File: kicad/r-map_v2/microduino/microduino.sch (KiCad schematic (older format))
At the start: 14 parts, among them P1 CONN_01X02, P2 CONN_RELE_BOARD, P3 CONN_01X05, P4 CONFIG, P5 USB_OTG, U1 Microduino, U2 ESDA6V1-5SC6, U3 LP2985LV, U4 TMP275

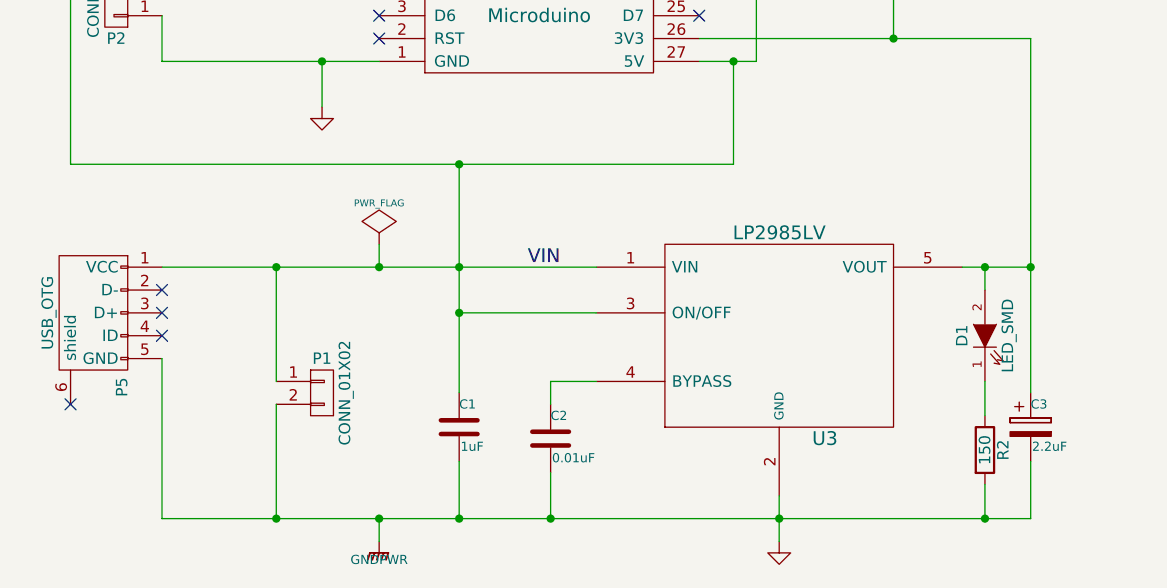
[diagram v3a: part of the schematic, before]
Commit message: Aggiunto ponticello a saldare per uscita 3.3V. Nuovo design per i2chub
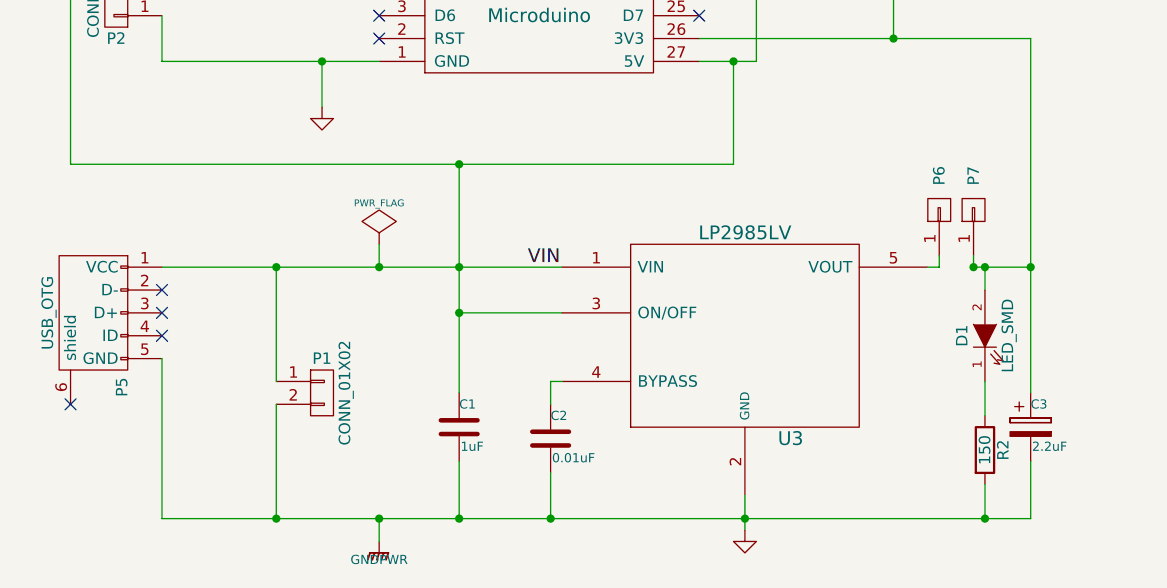
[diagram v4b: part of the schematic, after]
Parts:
- added P6, P7: CONN_01X01, Measurement_Points:Measurement_Point_Square-SMD-Pad_Small, symbol CONN_01X01
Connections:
- net +3.3V: now also P7.1 (P1); no longer U3.5 (VOUT)
- new net: P6.1 (P1), U3.5 (VOUT)
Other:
- moved on the sheet: U3
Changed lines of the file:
@@
 L LP2985LV U3
 U 1 1 548EC800
-P 5450 6400
-F 0 "U3" H 5650 5950 60  0000 C CNN
-F 1 "LP2985LV" H 5450 6850 60  0000 C CNN
-F 2 "w_smd_trans:sot23-5" H 5450 6400 60  0001 C CNN
-F 3 "http://www.ti.com/lit/ds/symlink/lp2985-n.pdf" H 5450 6400 60  0001 C CNN
-	1    5450 6400
+P 5300 6400
+F 0 "U3" H 5500 5950 60  0000 C CNN
+F 1 "LP2985LV" H 5300 6850 60  0000 C CNN
+F 2 "w_smd_trans:sot23-5" H 5300 6400 60  0001 C CNN
+F 3 "http://www.ti.com/lit/ds/symlink/lp2985-n.pdf" H 5300 6400 60  0001 C CNN
+	1    5300 6400
 	1    0    0    -1
 $EndComp
@@
 L GND #PWR01
 U 1 1 548ECA52
-P 5450 7300
-F 0 "#PWR01" H 5450 7300 30  0001 C CNN
-F 1 "GND" H 5450 7230 30  0001 C CNN
-F 2 "" H 5450 7300 60  0000 C CNN
-F 3 "" H 5450 7300 60  0000 C CNN
-	1    5450 7300
+P 5300 7250
+F 0 "#PWR01" H 5300 7250 30  0001 C CNN
+F 1 "GND" H 5300 7180 30  0001 C CNN
+F 2 "" H 5300 7250 60  0000 C CNN
+F 3 "" H 5300 7250 60  0000 C CNN
+	1    5300 7250
 	1    0    0    -1
 $EndComp
@@
 $EndComp
 NoConn ~ 3700 4500
-Wire Wire Line
-	2750 5200 3700 5200
-Wire Wire Line
-	4600 3750 4050 3750
-Wire Wire Line
-	4300 3750 4300 4000
-Wire Wire Line
-	2850 2900 5800 2900
-Wire Wire Line
-	4800 2750 4800 3250
-Wire Wire Line
-	5950 5100 5950 3250
-Wire Wire Line
-	3000 3550 2850 3550
-Wire Wire Line
-	4200 3550 4200 4000
-Wire Wire Line
-	2750 5200 2750 5000
-Wire Wire Line
-	2750 4900 3700 4900
-Wire Wire Line
-	3700 4800 2750 4800
-Wire Wire Line
-	2850 3550 2850 2900
-Wire Wire Line
-	5250 5650 5250 5200
-Wire Wire Line
-	2350 5650 5250 5650
-Wire Wire Line
-	2350 5650 2350 4400
-Wire Wire Line
-	2350 4400 2750 4400
-Wire Wire Line
-	2750 4400 2750 4500
-Wire Wire Line
-	4600 2750 4600 3750
-Wire Wire Line
-	4500 3550 4500 2750
-Wire Wire Line
-	4700 2900 4700 2750
-Wire Wire Line
-	4400 2750 4400 3350
-Wire Wire Line
-	4050 3350 5350 3350
-Wire Wire Line
-	5350 3350 5350 5200
-Connection ~ 5250 5200
-Wire Wire Line
-	5950 3250 4800 3250
-Wire Wire Line
-	4050 3550 4500 3550
-Connection ~ 4200 3550
-Connection ~ 4300 3750
-Wire Wire Line
-	4050 7200 4050 6950
-Wire Wire Line
-	2750 7200 6550 7200
-Wire Wire Line
-	6550 7200 6550 6950
-Wire Wire Line
-	5450 7100 5450 7300
-Connection ~ 5450 7200
-Wire Wire Line
-	6550 5100 6550 6650
-Wire Wire Line
-	4050 5650 4050 6650
-Wire Wire Line
-	2750 6100 4650 6100
-Wire Wire Line
-	4050 6300 4650 6300
-Connection ~ 4050 6300
-Wire Wire Line
-	6250 6100 6550 6100
-Connection ~ 4050 7200
-Connection ~ 4050 6100
-Wire Wire Line
-	3250 6600 3250 6100
-Connection ~ 3250 6100
-Wire Wire Line
-	3250 6700 3250 7200
-Connection ~ 3250 7200
-Wire Wire Line
-	4650 6600 4450 6600
-Wire Wire Line
-	4450 6600 4450 6700
-Wire Wire Line
-	4450 7000 4450 7200
-Connection ~ 4450 7200
-Connection ~ 6550 6100
-Wire Wire Line
-	3700 6000 3700 6100
-Connection ~ 3700 6100
-Wire Wire Line
-	3700 7300 3700 7200
-Connection ~ 3700 7200
-Wire Wire Line
-	5850 3000 4500 3000
-Connection ~ 4500 3000
-Wire Wire Line
-	5850 3150 4600 3150
-Connection ~ 4600 3150
-Wire Wire Line
-	5800 2900 5800 4400
-Wire Wire Line
-	7050 3850 5800 3850
-Connection ~ 4700 2900
-Wire Wire Line
-	3000 2800 5650 2800
-Wire Wire Line
-	5650 2800 5650 2550
-Wire Wire Line
-	5650 2550 6350 2550
-Wire Wire Line
-	6350 2550 6350 2600
-Connection ~ 4800 2800
-Wire Wire Line
-	6850 2900 7050 2900
-Wire Wire Line
-	7050 2900 7050 3850
-Connection ~ 6350 3850
-Wire Wire Line
-	6850 3000 7050 3000
-Connection ~ 7050 3000
-Wire Wire Line
-	6850 3100 7050 3100
-Wire Wire Line
-	5100 4900 5800 4900
-Connection ~ 5800 3850
-Connection ~ 4050 5650
-Wire Wire Line
-	3450 5200 3450 5400
-Connection ~ 3450 5200
-Wire Wire Line
-	5100 5100 6550 5100
-Wire Wire Line
-	5350 5200 5100 5200
-Wire Wire Line
-	6350 3750 6350 4000
 NoConn ~ 2750 6400
 $Comp
@@
 	0    -1   1    0
 $EndComp
-Wire Wire Line
-	2750 7200 2750 6500
 NoConn ~ 2350 6700
 $Comp
@@
 	1    0    0    -1
 $EndComp
-Wire Wire Line
-	6350 6750 6350 6600
-Wire Wire Line
-	6350 6200 6350 6100
-Connection ~ 6350 6100
-Wire Wire Line
-	6350 7050 6350 7200
-Connection ~ 6350 7200
 Text Label 4300 3550 0    60   ~ 0
 SCL
 Text Label 4400 3750 0    60   ~ 0
 SDA
-Connection ~ 7050 3100
 Text Label 5350 2800 0    60   ~ 0
 +3.3V
@@
 Text Label 4350 6100 0    60   ~ 0
 VIN
+NoConn ~ 3700 4600
+NoConn ~ 3700 4700
+Wire Wire Line
+	2750 5200 3700 5200
+Wire Wire Line
+	4600 3750 4050 3750
+Wire Wire Line
+	4300 3750 4300 4000
+Wire Wire Line
+	2850 2900 5800 2900
+Wire Wire Line
+	4800 2750 4800 3250
+Wire Wire Line
+	5950 5100 5950 3250
+Wire Wire Line
+	3000 3550 2850 3550
+Wire Wire Line
+	4200 3550 4200 4000
+Wire Wire Line
+	2750 5200 2750 5000
+Wire Wire Line
+	2750 4900 3700 4900
+Wire Wire Line
+	3700 4800 2750 4800
+Wire Wire Line
+	2850 3550 2850 2900
+Wire Wire Line
+	5250 5650 5250 5200
+Wire Wire Line
+	2350 5650 5250 5650
+Wire Wire Line
+	2350 5650 2350 4400
+Wire Wire Line
+	2350 4400 2750 4400
+Wire Wire Line
+	2750 4400 2750 4500
+Wire Wire Line
+	4600 2750 4600 3750
+Wire Wire Line
+	4500 3550 4500 2750
+Wire Wire Line
+	4700 2900 4700 2750
+Wire Wire Line
+	4400 2750 4400 3350
+Wire Wire Line
+	4050 3350 5350 3350
+Wire Wire Line
+	5350 3350 5350 5200
+Connection ~ 5250 5200
+Wire Wire Line
+	5950 3250 4800 3250
+Wire Wire Line
+	4050 3550 4500 3550
+Connection ~ 4200 3550
+Connection ~ 4300 3750
+Wire Wire Line
+	4050 7200 4050 6950
+Wire Wire Line
+	2750 7200 6550 7200
+Wire Wire Line
+	6550 7200 6550 6950
+Wire Wire Line
+	5300 7100 5300 7250
+Connection ~ 5300 7200
+Wire Wire Line
+	6550 5100 6550 6650
+Wire Wire Line
+	4050 5650 4050 6650
+Wire Wire Line
+	2750 6100 4500 6100
+Wire Wire Line
+	4050 6300 4500 6300
+Connection ~ 4050 6300
+Connection ~ 4050 7200
+Connection ~ 4050 6100
+Wire Wire Line
+	3250 6600 3250 6100
+Connection ~ 3250 6100
+Wire Wire Line
+	3250 6700 3250 7200
+Connection ~ 3250 7200
+Wire Wire Line
+	4500 6600 4450 6600
+Wire Wire Line
+	4450 6600 4450 6700
+Wire Wire Line
+	4450 7000 4450 7200
+Connection ~ 4450 7200
+Connection ~ 6550 6100
+Wire Wire Line
+	3700 6000 3700 6100
+Connection ~ 3700 6100
+Wire Wire Line
+	3700 7300 3700 7200
+Connection ~ 3700 7200
+Wire Wire Line
+	5850 3000 4500 3000
+Connection ~ 4500 3000
+Wire Wire Line
+	5850 3150 4600 3150
+Connection ~ 4600 3150
+Wire Wire Line
+	5800 2900 5800 4400
+Wire Wire Line
+	7050 3850 5800 3850
+Connection ~ 4700 2900
+Wire Wire Line
+	3000 2800 5650 2800
+Wire Wire Line
+	5650 2800 5650 2550
+Wire Wire Line
+	5650 2550 6350 2550
+Wire Wire Line
+	6350 2550 6350 2600
+Connection ~ 4800 2800
+Wire Wire Line
+	6850 2900 7050 2900
+Wire Wire Line
+	7050 2900 7050 3850
+Connection ~ 6350 3850
+Wire Wire Line
+	6850 3000 7050 3000
+Connection ~ 7050 3000
+Wire Wire Line
+	6850 3100 7050 3100
+Wire Wire Line
+	5100 4900 5800 4900
+Connection ~ 5800 3850
+Connection ~ 4050 5650
+Wire Wire Line
+	3450 5200 3450 5400
+Connection ~ 3450 5200
+Wire Wire Line
+	5100 5100 6550 5100
+Wire Wire Line
+	5350 5200 5100 5200
+Wire Wire Line
+	6350 3750 6350 4000
+Wire Wire Line
+	2750 7200 2750 6500
+Wire Wire Line
+	6350 6750 6350 6600
+Wire Wire Line
+	6350 6200 6350 6100
+Connection ~ 6350 6100
+Wire Wire Line
+	6350 7050 6350 7200
+Connection ~ 6350 7200
+Connection ~ 7050 3100
 Connection ~ 5950 5100
 Connection ~ 4400 3350
@@
 Wire Wire Line
 	3550 4600 2750 4600
-NoConn ~ 3700 4600
-NoConn ~ 3700 4700
+$Comp
+L CONN_01X01 P6
+U 1 1 55F70AFE
+P 6150 5850
+F 0 "P6" H 6300 5850 50  0000 C CNN
+F 1 "CONN_01X01" V 6250 5850 50  0001 C CNN
+F 2 "Measurement_Points:Measurement_Point_Square-SMD-Pad_Small" H 6150 5850 60  0001 C CNN
+F 3 "" H 6150 5850 60  0000 C CNN
+	1    6150 5850
+	0    -1   -1   0
+$EndComp
+$Comp
+L CONN_01X01 P7
+U 1 1 55F70BDA
+P 6300 5850
+F 0 "P7" H 6450 5850 50  0000 C CNN
+F 1 "CONN_01X01" V 6400 5850 50  0001 C CNN
+F 2 "Measurement_Points:Measurement_Point_Square-SMD-Pad_Small" H 6300 5850 60  0001 C CNN
+F 3 "" H 6300 5850 60  0000 C CNN
+	1    6300 5850
+	0    -1   -1   0
+$EndComp
+Wire Wire Line
+	6300 6050 6300 6100
+Connection ~ 6300 6100
+Wire Wire Line
+	6150 6050 6150 6100
+Wire Wire Line
+	6150 6100 6100 6100
+Wire Wire Line
+	6300 6100 6550 6100
 $EndSCHEMATC

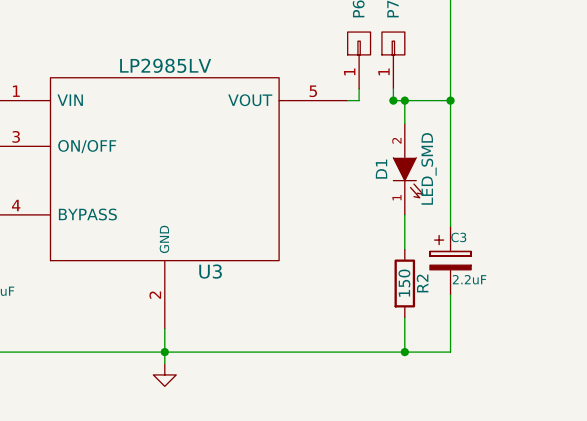
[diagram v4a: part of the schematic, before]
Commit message: Aggiornamento files gerber e verifica per nuova stampa pcb, revisionate tutte e 4 le board. Il file kicad/r-map_v2/futura_10-2015.zip contiene i files divisi per cartelle di tutte le board
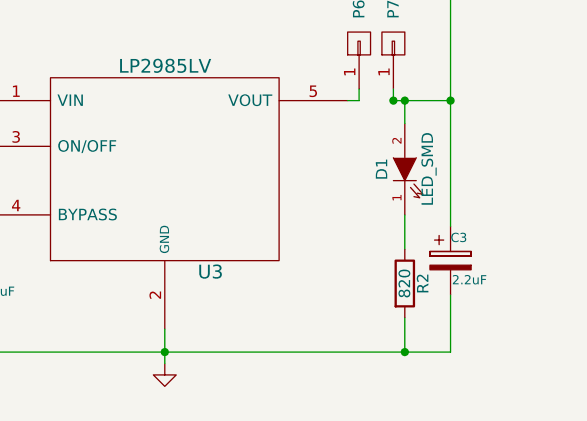
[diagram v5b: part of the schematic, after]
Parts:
- R2: value 150 -> 820
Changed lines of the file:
@@
 P 6350 6900
 F 0 "R2" V 6430 6900 50  0000 C CNN
-F 1 "150" V 6350 6900 50  0000 C CNN
+F 1 "820" V 6350 6900 50  0000 C CNN
 F 2 "w_smd_resistors:r_1206" V 6280 6900 30  0001 C CNN
 F 3 "" H 6350 6900 30  0000 C CNN

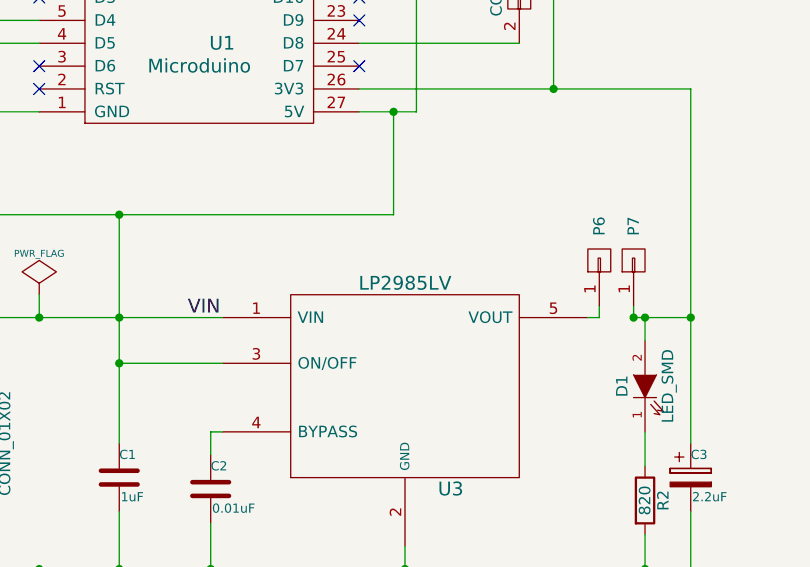
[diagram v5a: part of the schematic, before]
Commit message: Aggiornamento lista componenti e cancellazione vecchi files
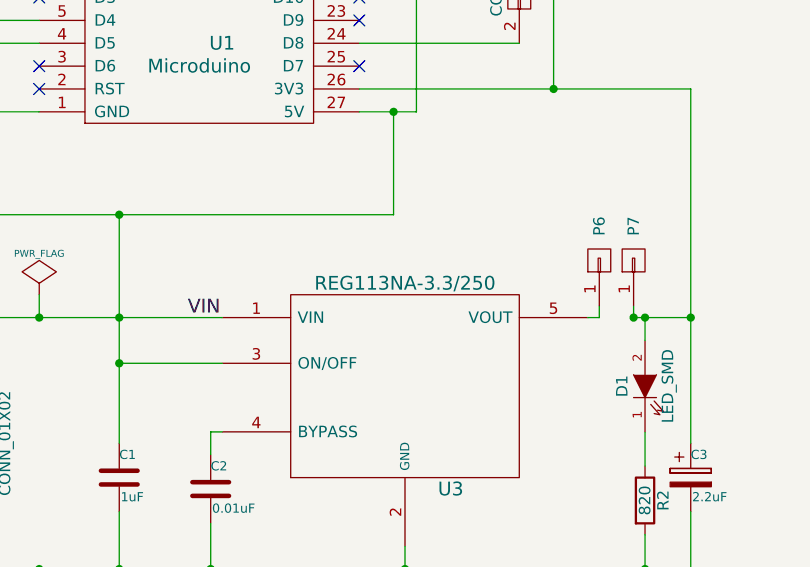
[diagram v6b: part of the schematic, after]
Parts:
- U3: value LP2985LV -> REG113NA-3.3/250
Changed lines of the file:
@@
 P 5300 6400
 F 0 "U3" H 5500 5950 60  0000 C CNN
-F 1 "LP2985LV" H 5300 6850 60  0000 C CNN
+F 1 "REG113NA-3.3/250" H 5300 6850 60  0000 C CNN
 F 2 "w_smd_trans:sot23-5" H 5300 6400 60  0001 C CNN
-F 3 "http://www.ti.com/lit/ds/symlink/lp2985-n.pdf" H 5300 6400 60  0001 C CNN
+F 3 "http://it.farnell.com/harwin/d01-9973242/socket-sil-32-vie-circuito-pc/dp/Search?storeId=10165&catalogId=15001&categoryId=&categoryName=&langId=-4&st=REG113NA-3.3%2F250" H 5300 6400 60  0001 C CNN
 	1    5300 6400
 	1    0    0    -1

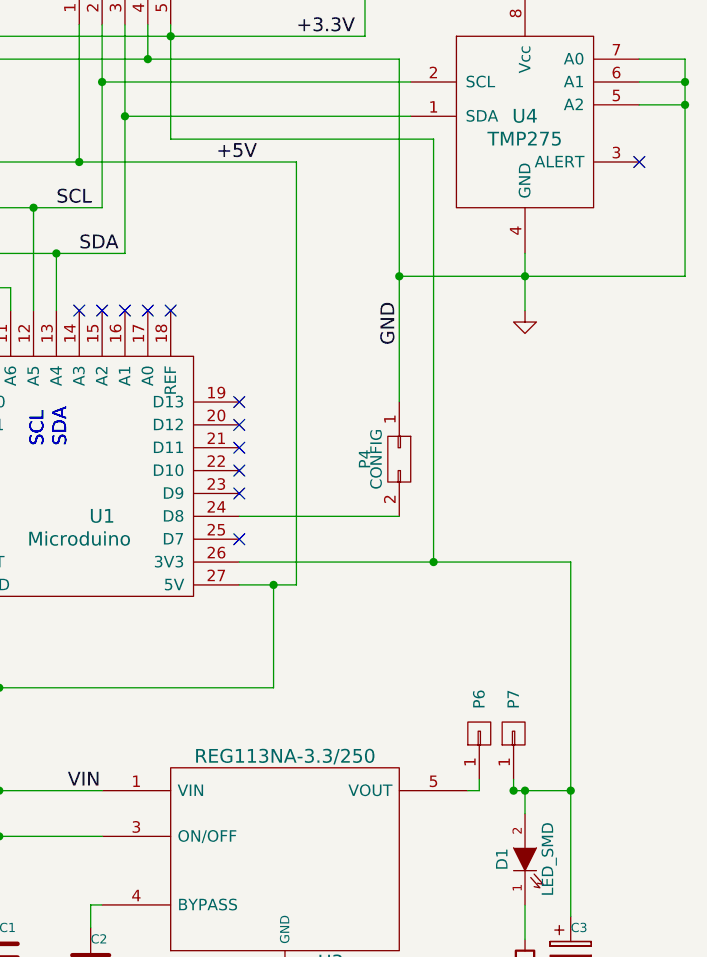
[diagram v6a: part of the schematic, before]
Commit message: Nouva versione pcb, doppia schermatura, allargamento piste, rimozione connessioni T ed Y
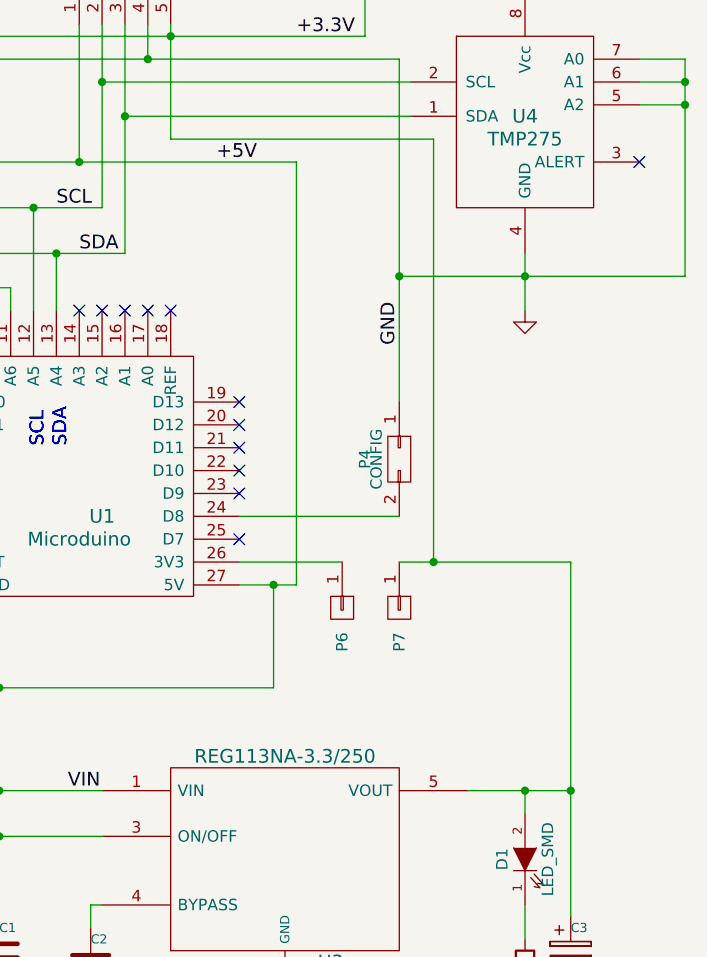
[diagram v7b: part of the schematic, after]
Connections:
- net +3.3V: now also U3.5 (VOUT); no longer U1.26 (3V3)
- net at P6.1 (P1): now also U1.26 (3V3); no longer U3.5 (VOUT)
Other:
- moved on the sheet: P6, P7
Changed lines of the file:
@@
 	4050 3350 5350 3350
 Wire Wire Line
-	5350 3350 5350 5200
+	5350 5200 5350 3350
 Connection ~ 5250 5200
 Wire Wire Line
@@
 Connection ~ 3450 5200
 Wire Wire Line
-	5100 5100 6550 5100
-Wire Wire Line
-	5350 5200 5100 5200
+	5100 5200 5350 5200
 Wire Wire Line
 	6350 3750 6350 4000
@@
 L CONN_01X01 P6
 U 1 1 55F70AFE
-P 6150 5850
-F 0 "P6" H 6300 5850 50  0000 C CNN
-F 1 "CONN_01X01" V 6250 5850 50  0001 C CNN
-F 2 "Measurement_Points:Measurement_Point_Square-SMD-Pad_Small" H 6150 5850 60  0001 C CNN
-F 3 "" H 6150 5850 60  0000 C CNN
-	1    6150 5850
-	0    -1   -1   0
+P 5550 5300
+F 0 "P6" H 5700 5300 50  0000 C CNN
+F 1 "CONN_01X01" V 5650 5300 50  0001 C CNN
+F 2 "Measurement_Points:Measurement_Point_Square-SMD-Pad_Small" H 5550 5300 60  0001 C CNN
+F 3 "" H 5550 5300 60  0000 C CNN
+	1    5550 5300
+	0    1    1    0
 $EndComp
 $Comp
 L CONN_01X01 P7
 U 1 1 55F70BDA
-P 6300 5850
-F 0 "P7" H 6450 5850 50  0000 C CNN
-F 1 "CONN_01X01" V 6400 5850 50  0001 C CNN
-F 2 "Measurement_Points:Measurement_Point_Square-SMD-Pad_Small" H 6300 5850 60  0001 C CNN
-F 3 "" H 6300 5850 60  0000 C CNN
-	1    6300 5850
-	0    -1   -1   0
+P 5800 5300
+F 0 "P7" H 5950 5300 50  0000 C CNN
+F 1 "CONN_01X01" V 5900 5300 50  0001 C CNN
+F 2 "Measurement_Points:Measurement_Point_Square-SMD-Pad_Small" H 5800 5300 60  0001 C CNN
+F 3 "" H 5800 5300 60  0000 C CNN
+	1    5800 5300
+	0    1    1    0
 $EndComp
 Wire Wire Line
-	6300 6050 6300 6100
-Connection ~ 6300 6100
+	6550 6100 6100 6100
 Wire Wire Line
-	6150 6050 6150 6100
+	5800 5100 6550 5100
 Wire Wire Line
-	6150 6100 6100 6100
-Wire Wire Line
-	6300 6100 6550 6100
+	5100 5100 5550 5100
 $EndSCHEMATC

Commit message: Aggiunti gerber files per breakout board e sistemato case led stima-i2c
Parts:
- D1: footprint w_smd_leds:Led_1206 -> w_smd_leds:Led_0805
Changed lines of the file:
@@
 F 0 "D1" H 6350 6500 50  0000 C CNN
 F 1 "LED_SMD" H 6350 6300 50  0000 C CNN
-F 2 "w_smd_leds:Led_1206" H 6350 6400 60  0001 C CNN
+F 2 "w_smd_leds:Led_0805" H 6350 6400 60  0001 C CNN
 F 3 "" H 6350 6400 60  0000 C CNN
 	1    6350 6400
@@
 	4050 3350 5350 3350
 Wire Wire Line
-	5350 5200 5350 3350
+	5350 3350 5350 5200
 Connection ~ 5250 5200
 Wire Wire Line
@@
 Connection ~ 3450 5200
 Wire Wire Line
-	5100 5200 5350 5200
+	5350 5200 5100 5200
 Wire Wire Line
 	6350 3750 6350 4000
